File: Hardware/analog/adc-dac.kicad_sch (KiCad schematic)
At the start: 18 parts, among them U601 MCP3562, U602 MAX6166, U603 DAC8562

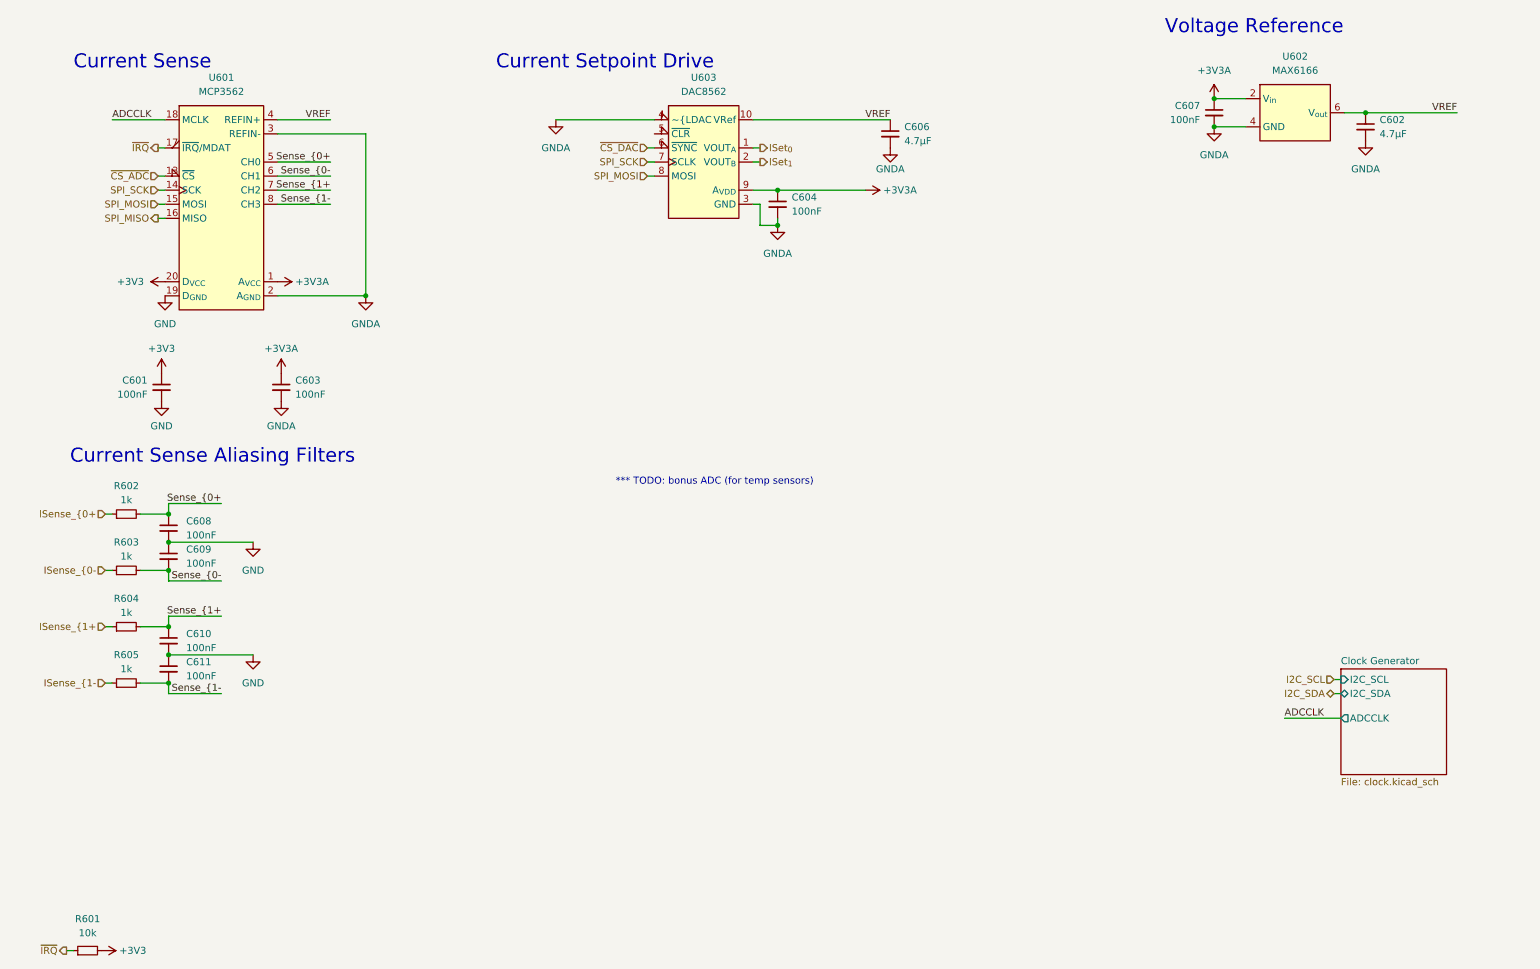
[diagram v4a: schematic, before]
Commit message: Added more decoupling for reference
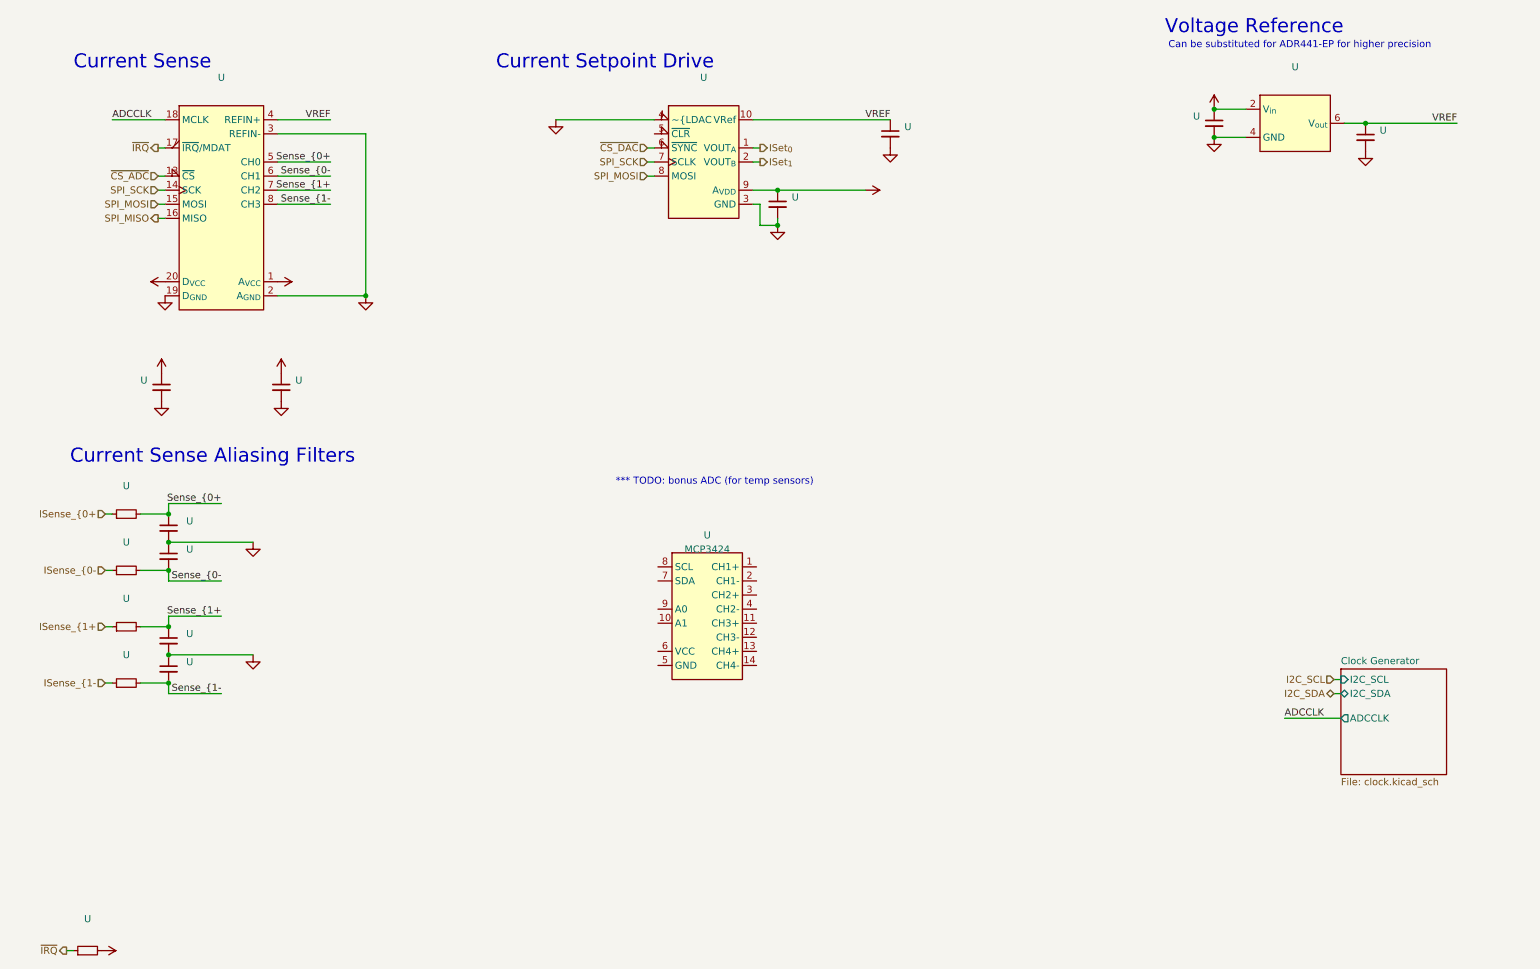
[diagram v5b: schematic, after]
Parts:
- added U: MCP3424, Package_SO:SOIC-14_3.9x8.7mm_P1.27mm, symbol programmable-load:MCP3424
- U: renamed from R602; value 1k -> (none); footprint Resistor_SMD:R_0805_2012Metric_Pad1.20x1.40mm_HandSolder -> (none)
- U: renamed from R603; value 1k -> (none); footprint Resistor_SMD:R_0805_2012Metric_Pad1.20x1.40mm_HandSolder -> (none)
- U: renamed from R605; value 1k -> (none); footprint Resistor_SMD:R_0805_2012Metric_Pad1.20x1.40mm_HandSolder -> (none)
- U: renamed from C606; value 4.7µF -> (none); footprint Capacitor_SMD:C_0805_2012Metric_Pad1.18x1.45mm_HandSolder -> (none)
- U: renamed from U603; value DAC8562 -> (none); footprint Package_SO:MSOP-10_3x3mm_P0.5mm -> (none)
- U: renamed from U601; value MCP3562 -> (none); footprint Package_SO:TSSOP-20_4.4x6.5mm_P0.65mm -> (none)
- U: renamed from C609; value 100nF -> (none); footprint Capacitor_SMD:C_0805_2012Metric_Pad1.18x1.45mm_HandSolder -> (none)
- U: renamed from C603; value 100nF -> (none); footprint Capacitor_SMD:C_0805_2012Metric_Pad1.18x1.45mm_HandSolder -> (none)
- U: renamed from C602; value 4.7µF -> (none); footprint Capacitor_SMD:C_0805_2012Metric_Pad1.18x1.45mm_HandSolder -> (none)
- U: renamed from C607; value 100nF -> (none); footprint Capacitor_SMD:C_0805_2012Metric_Pad1.18x1.45mm_HandSolder -> (none)
- U: renamed from R601; value 10k -> (none); footprint Resistor_SMD:R_0805_2012Metric_Pad1.20x1.40mm_HandSolder -> (none)
- U: renamed from C608; value 100nF -> (none); footprint Capacitor_SMD:C_0805_2012Metric_Pad1.18x1.45mm_HandSolder -> (none)
- U: renamed from C604; value 100nF -> (none); footprint Capacitor_SMD:C_0805_2012Metric_Pad1.18x1.45mm_HandSolder -> (none)
- U: renamed from U602; value MAX6166 -> (none); footprint Package_SO:SOIC-8_3.9x4.9mm_P1.27mm -> (none)
- U: renamed from R604; value 1k -> (none); footprint Resistor_SMD:R_0805_2012Metric_Pad1.20x1.40mm_HandSolder -> (none)
- U: renamed from C601; value 100nF -> (none); footprint Capacitor_SMD:C_0805_2012Metric_Pad1.18x1.45mm_HandSolder -> (none)
- U: renamed from C611; value 100nF -> (none); footprint Capacitor_SMD:C_0805_2012Metric_Pad1.18x1.45mm_HandSolder -> (none)
- U: renamed from C610; value 100nF -> (none); footprint Capacitor_SMD:C_0805_2012Metric_Pad1.18x1.45mm_HandSolder -> (none)
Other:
- note added: "Can be substituted for ADR441-EP for higher precision"
- moved on the sheet: U

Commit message: Analog board layout
- Started work on adding the voltage sense circuitry, including the
  selector relay, IO expander to drive the relay, and the second ADC to
  convert the voltage values

- Changed the layout of analog board to better take advantage of
  available space

- Minor changes to front panel layout for aesthetics
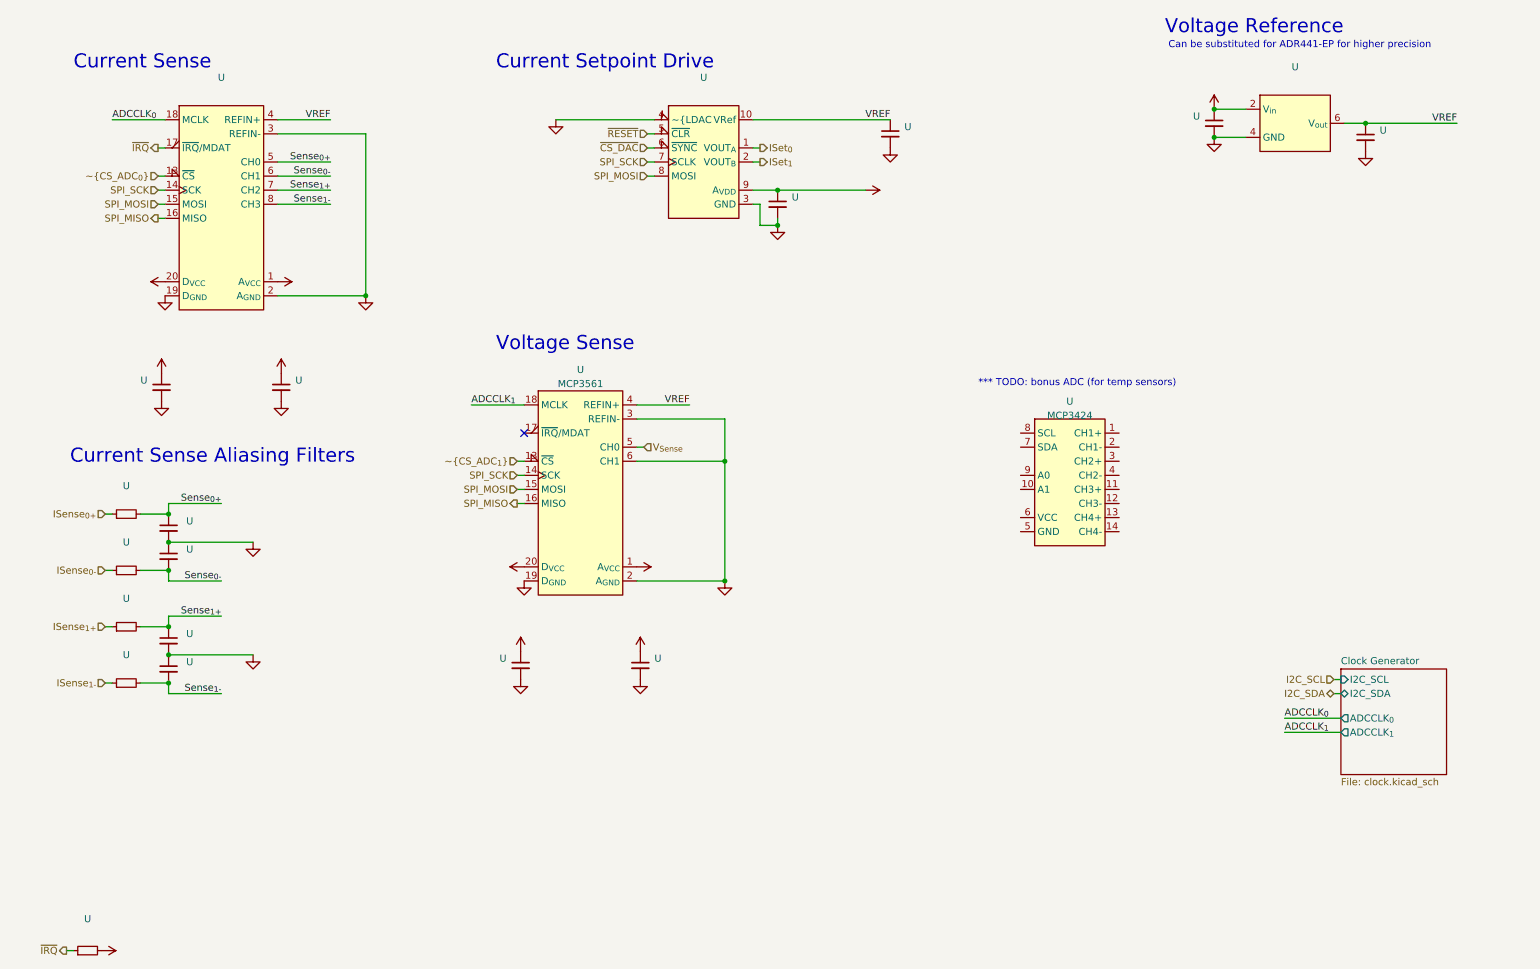
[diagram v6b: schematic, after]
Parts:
- added U: MCP3561, Package_SO:TSSOP-20_4.4x6.5mm_P0.65mm, symbol programmable-load:MCP3561
- added U (x2): (no value), symbol Device:C_Small
- U: MPN CL21A475KAQNNNF -> (none)
- U: MPN RMC1/10-103JTP -> (none)
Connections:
- net +3V3: now also U.1, U.20 (D_{VCC})
- net +3V3A: now also U.1, U.1 (A_{VCC})
- net GND: now also U.19 (D_{GND}), U.2
- net GNDA: now also U.2, U.2 (A_{GND}), U.3 (REFIN-), U.6 (CH1)
- net SPI_MISO: now also U.16 (MISO)
- net SPI_MOSI: now also U.15 (MOSI)
- net SPI_SCK: now also U.14 (SCK)
- net VREF: now also U.4 (REFIN+)
- net ~{RESET}: now reaches U.5 (~{CLR})
- net ADCCLK renamed ADCCLK_{0}
- net ISense_{0+ renamed ISense_{0+}
- net ISense_{0- renamed ISense_{0-}
- net ISense_{1+ renamed ISense_{1+}
- net ISense_{1- renamed ISense_{1-}
- net Sense_{0+ renamed Sense_{0+}
- net Sense_{0- renamed Sense_{0-}
- net Sense_{1+ renamed Sense_{1+}
- net Sense_{1- renamed Sense_{1-}
- net ~{CS_ADC} renamed ~{CS_ADC_{0}}
- new net ADCCLK_{1}: U.18 (MCLK)
- new net V_{Sense}: U.5 (CH0)
- new net ~{CS_ADC_{1}}: U.13 (~{CS})
- no-connect marks 0 -> 1
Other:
- sheet Clock Generator ports: added ADCCLK_{0}, ADCCLK_{1}; removed ADCCLK
- note added: "Voltage Sense"
- moved on the sheet: U

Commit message: Mostly finished up analog load board
- Finished routing most signals

- Connected relay drive to bonus I2C GPIO controller, and routed the
  rest of the voltage sense stuff

- Routed the reset signal to the DAC, so that when the board is reset,
  the current output will be reset to zero as well without processor
  intervention

- Replaced most passives with 0603/1608 size
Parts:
- U: MPN CR0805-JW-102ELF -> (none)
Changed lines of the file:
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@@
       (effects (font (size 1.27 1.27)) hide)
     )
-    (property "MPN" "CR0805-JW-102ELF" (id 4) (at 34.925 105.41 90)
+    (property "MPN" "" (id 4) (at 34.925 105.41 90)
       (effects (font (size 1.27 1.27)) hide)
     )
@@
       (effects (font (size 1.27 1.27)) hide)
     )
-    (property "MPN" "CR0805-JW-102ELF" (id 4) (at 34.925 115.57 90)
+    (property "MPN" "" (id 4) (at 34.925 115.57 90)
       (effects (font (size 1.27 1.27)) hide)
     )
@@
       (effects (font (size 1.27 1.27)) hide)
     )
-    (property "MPN" "CR0805-JW-102ELF" (id 4) (at 34.925 135.89 90)
+    (property "MPN" "" (id 4) (at 34.925 135.89 90)
       (effects (font (size 1.27 1.27)) hide)
     )
@@
       (effects (font (size 1.27 1.27)) hide)
     )
-    (property "MPN" "CR0805-JW-102ELF" (id 4) (at 34.925 125.73 90)
-      (effects (font (size 1.27 1.27)) hide)
-    )
+    (property "MPN" "" (id 4) (at 34.925 125.73 90)
+      (effects (font (size 1.27 1.27)) hide)
+    )

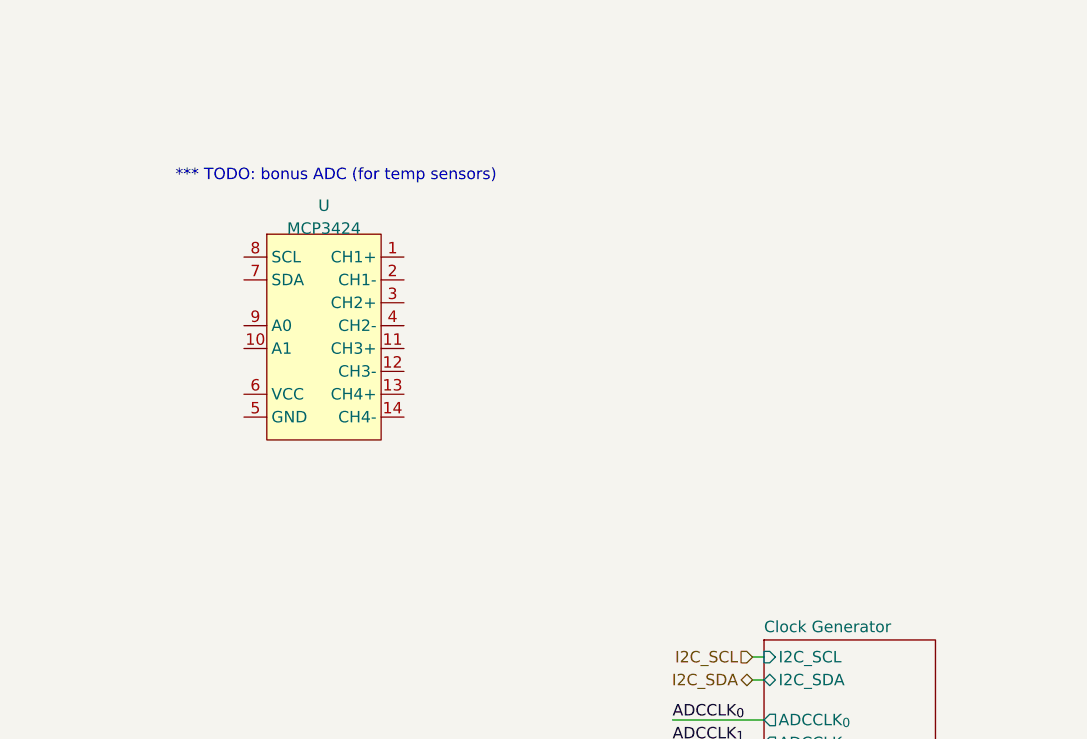
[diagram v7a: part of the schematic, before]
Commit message: Temperature sensing & cleanup for analog board
- Added the auxiliary temperature sensing ADC, and routed it to the
  analog temperature sensors on the front and rear of the MOSFET
  heatsink

- Added an LM75 sensor to measure the analog board ambient temperature
  (for better temperature control/fan control)

  This may end up being a DNP item if it's not really useful or
  otherwise necessary.

- Fixes to a few symbols (namely pin directions) to pass ERC
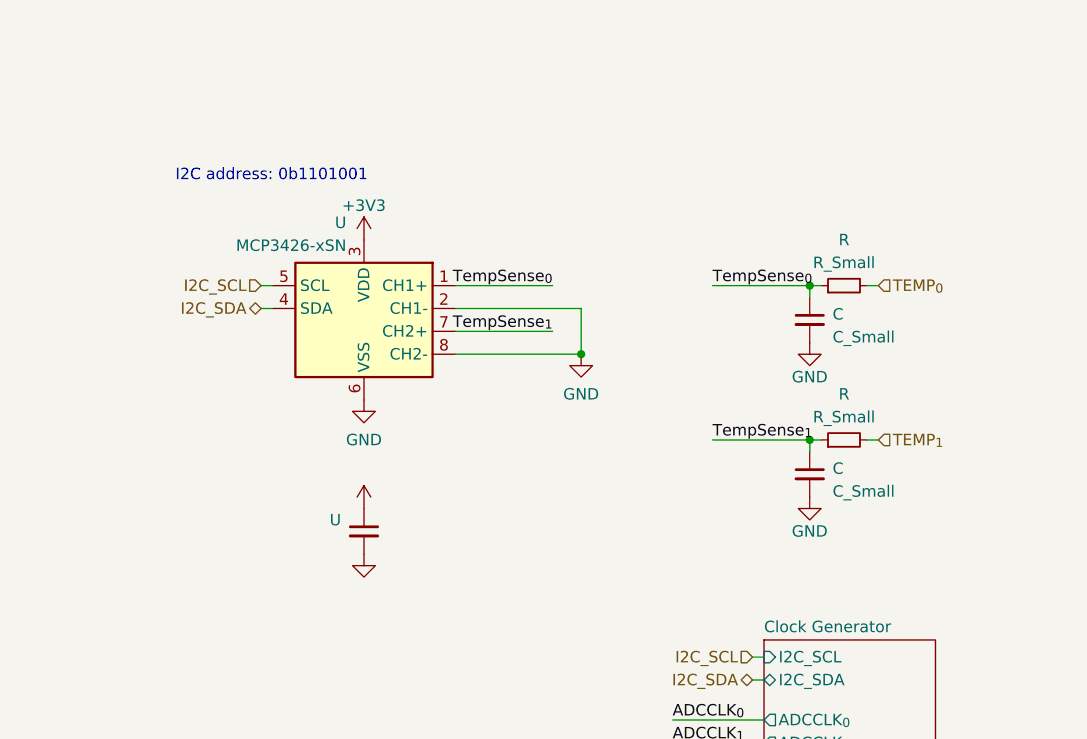
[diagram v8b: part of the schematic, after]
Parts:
- removed U: MCP3424, Package_SO:SOIC-14_3.9x8.7mm_P1.27mm, symbol programmable-load:MCP3424
- added C (x2): C_Small, symbol Device:C_Small
- added R (x2): R_Small, symbol Device:R_Small
- added U: (no value), symbol Device:C_Small
- added U: MCP3426-xSN, symbol Analog_ADC:MCP3426-xSN
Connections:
- net +3V3: now also U.1, U.3 (VDD)
- net GND: now also C.2, C.2, U.2, U.2 (CH1-), U.6 (VSS), U.8 (CH2-)
- net I2C_SCL: now also U.5 (SCL)
- net I2C_SDA: now also U.4 (SDA)
- new net TEMP_{0}: R.2
- new net TEMP_{1}: R.2
- new net TempSense_{0}: C.1, R.1, U.1 (CH1+)
- new net TempSense_{1}: C.1, R.1, U.7 (CH2+)
- now unconnected: U.1, U.3, U.5, U.7, U.8
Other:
- note added: "I2C address: 0b1101001"
- note removed: "*** TODO: bonus ADC (for temp sensors)"
